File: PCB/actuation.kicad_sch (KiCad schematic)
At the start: 10 parts, among them U2 MCP4725xxx-xCH, U4 TCA0372_DWG, U7 MCP4725xxx-xCH, U8 TCA0372_DWG

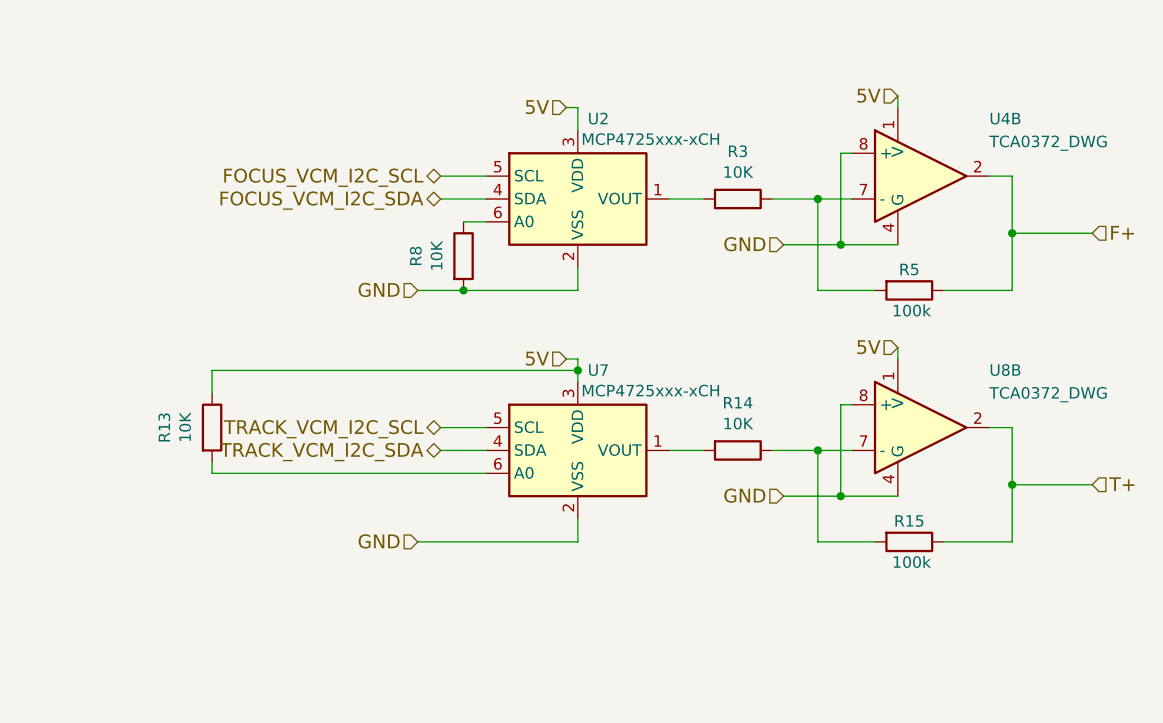
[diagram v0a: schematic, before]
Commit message: Update schematic based on testing
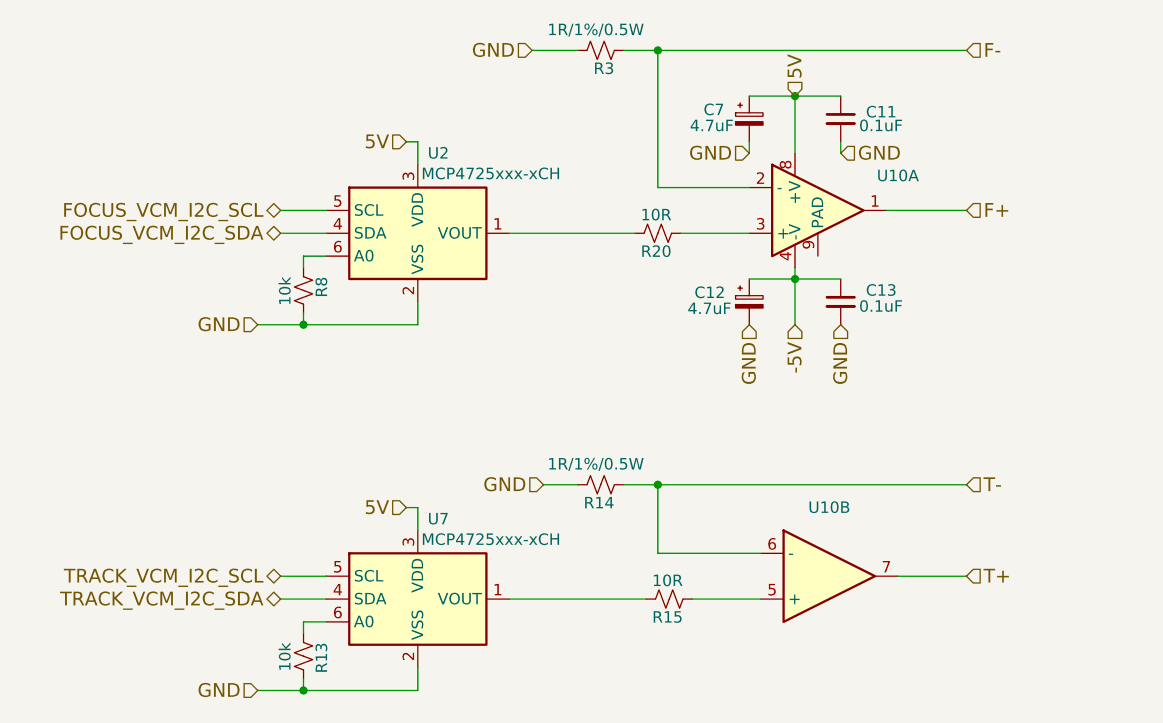
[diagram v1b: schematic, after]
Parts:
- removed R13, R14, R3, R8: 10K, GaudiLabsFootPrints:0805G, symbol DVDLaserScanner-rescue:R
- removed R15, R5: 100k, GaudiLabsFootPrints:0805G, symbol DVDLaserScanner-rescue:R
- removed U4, U8: TCA0372_DWG, GaudiLabsFootPrints:SO-16-W, symbol DVDLaserScanner-rescue:TCA0372_DWG
- added C11, C13: 0.1uF, symbol DVDLaserScanner-rescue:C_Small
- added C12, C7: 4.7uF, symbol DVDLaserScanner-rescue:CP_Small
- added R13, R8: 10k, symbol Device:R_Small_US
- added R14, R3: 1R/1%/0.5W, symbol Device:R_Small_US
- added R15, R20: 10R, symbol Device:R_Small_US
- added U10: ~, Package_SO:SOIC-8-1EP_3.9x4.9mm_P1.27mm_EP2.29x3mm, symbol AD8937:AD8397
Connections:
- net 5V: now also C11.1, C7.1, U10.8 (+V)
- net F+: now also U10.1
- net GND: now also C11.2, C12.2, C13.2, C7.2, R13.1, R14.1, R3.1, R8.1
- net T+: now also U10.7
- net at U2.6 (A0): now also R8.2
- net at U7.1 (VOUT): now also R15.1
- net at U7.6 (A0): now also R13.2
- net at U2.1 (VOUT): now also R20.1
- new net: R15.2, U10.5 (+)
- new net: R20.2, U10.3 (+)
- new net -5V: C12.1, C13.1, U10.4 (-V)
- new net F-: R3.2, U10.2 (-)
- new net T-: R14.2, U10.6 (-)
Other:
- moved on the sheet: U2
